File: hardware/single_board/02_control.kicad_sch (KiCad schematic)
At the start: 30 parts, among them U7 RP2350A, U8 W25Q128JVUXIQ, U9 SPX3819M5-3.3, Y1 12MHz

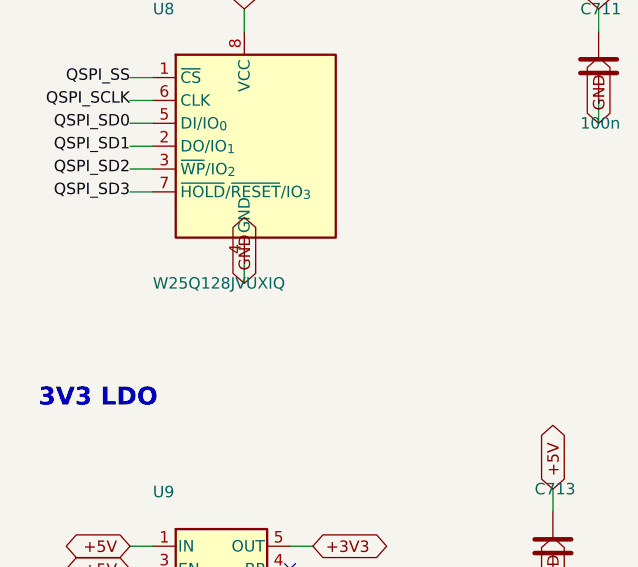
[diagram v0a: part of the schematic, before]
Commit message: Every placed part gets an LCSC number; 3D inductors and part colours fixed
LCSC (hardware/parts/lcsc.csv, 76 rows): every part the assembler places on
boards A (120) and S (173) now has a number, joined into the 3D part pane.
Chosen from the sister board's BOM where it had the part, JLC basic parts
where the rating allowed, each matched to the net it sits on and checked
against JLCPCB's library (model, package, rating, stock) on 2026-09-24. The
notes say why where it was not obvious: 100 V X7R/C0G on VBUS, 0.1% thin
film for the dividers, a Vishay WSL metal-strip jumper for phase C's 0R
(75 A, where a thick-film 0R carries a few), a CL 20 pF crystal for the
27 pF caps, the RGB LED placed rotated 180 deg. export_3d.py warns about any
placed part without a number; copper features (lands, lead pads, bosses)
get no LCSC row in the pane.

Two values changed because nothing stocked matches them:
- Shunts 1m6 -> 2m0 (WSLP20102L000FEA): no 1.6 mOhm 2010 exists at LCSC or
  JLCPCB. The pair is 1.0 mOhm, 50 mV/A, +-29.0 A worst case -- 2.5% over
  the 28.3 A peak, the margin draft 0.3 turned down, taken knowingly.
  geometry.SHUNT_EACH follows; spec, README and status page re-derive the
  sense chain and the loss budget (10.72 W, <= 6.67 K/W, >= 100 cm2).
- Flash W25Q128 -> W25Q16JVUXIQ: no 128 Mbit part comes in USON 2x3; this
  is the RP2350 reference design's part. Derived symbol renamed W25Q16JV.
Schematics regenerated in a scratch copy and only the changed sheets copied
back (diffed: nothing else moved); the routed boards' value fields patched
in place. ERC 0 and DRC 0 on both; KiCad's parity list is HEAD's minus one
(board A's U8 value mismatch). Board S's plan drawings and parts table
regenerated, which also brings them back in line with the final placement.

3D export:
- Board S's two buck inductors were invisible: kicad-cli 9.0.8 meshes a STEP
  that is an assembly of sub-assemblies (KiCad's own SWPA4030S) as empty
  nodes, silently. tools/flatten_step.py flattens it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
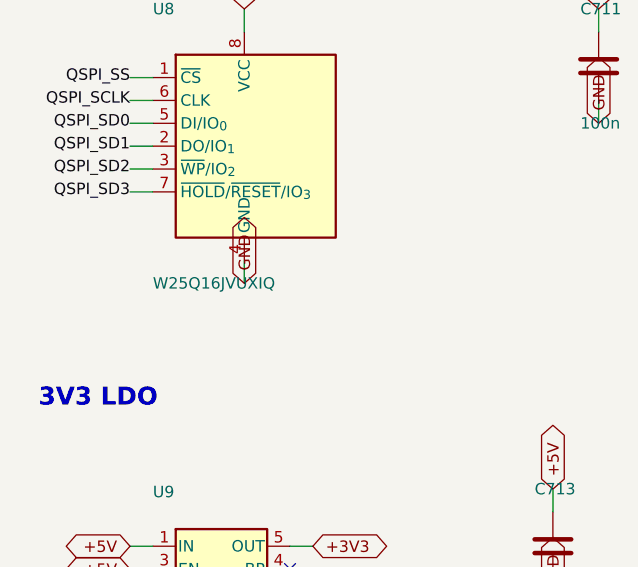
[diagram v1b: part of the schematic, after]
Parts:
- U8: value W25Q128JVUXIQ -> W25Q16JVUXIQ; symbol servodrive:W25Q128JV -> servodrive:W25Q16JV
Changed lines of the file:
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@@
 )
 	(symbol
-		(lib_id "servodrive:W25Q128JV")
+		(lib_id "servodrive:W25Q16JV")
 		(at 38.1000 355.6000 0)
 		(unit 1)
@@
 			(at 27.9400 340.3600 0)
 			(effects (font (size 1.27 1.27)) (justify left)))
-		(property "Value" "W25Q128JVUXIQ"
+		(property "Value" "W25Q16JVUXIQ"
 			(at 27.9400 370.8400 0)
 			(effects (font (size 1.27 1.27)) (justify left)))

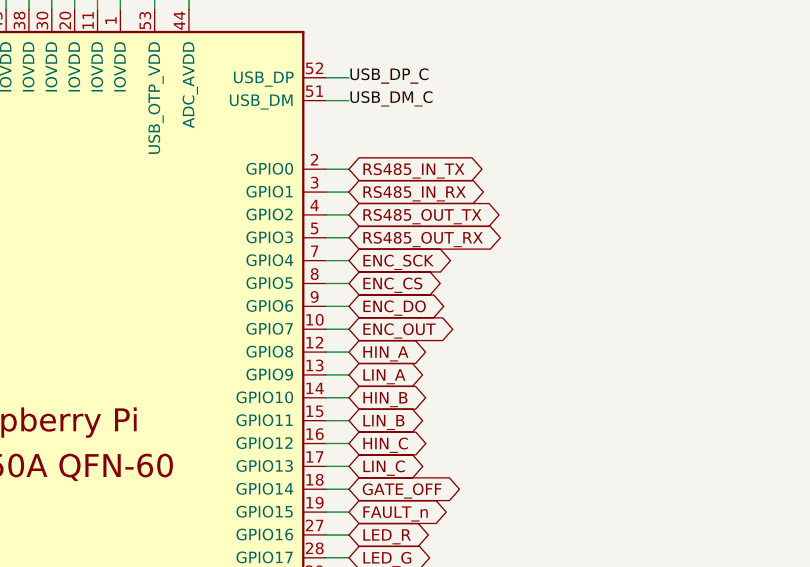
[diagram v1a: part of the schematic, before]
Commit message: Board S: screw keepouts, finer In3 centre rules, encoder on SPI0 (WIP, unrouted)
Work in progress from 2026-09-24/25, saved before routing is finished.
The board file here is the generator's output, not a routed board.

- Keepouts on F.Cu and B.Cu round the four centre motor screws
- USB-C placed tangent to the edge
- Encoder on SPI0 (ENC_DO GPIO4, ENC_SCK GPIO6); J13 pins swapped
- C901 moved north; encoder stitching vias back in the chip's pads
- "fine centre" rule area: signal nets on In3 inside R 17 may use
  0.12 mm track and clearance (servodrive_S.kicad_dru); finish.py's
  maze tries 0.12 there when 0.15 fails; the area is stripped before
  the DSN export so freerouting doesn't see it as a keepout
- Footprint tweaks: 0402 small pads, L_pol_2016, RP2350 QFN

Co-Authored-By: Claude Opus 5.5 (1M context) <noreply@anthropic.com>
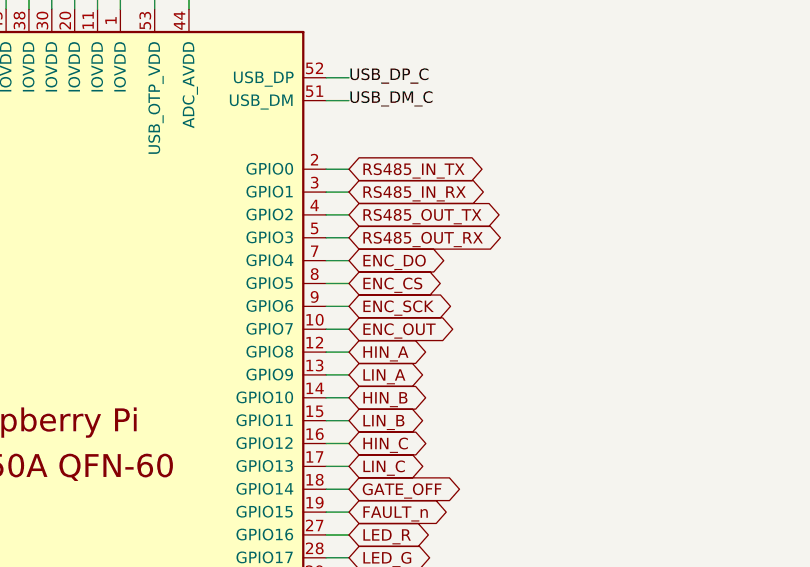
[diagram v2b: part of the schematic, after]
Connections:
- net ENC_DO: now also U7.7 (GPIO4); no longer U7.9 (GPIO6)
- net ENC_SCK: now also U7.9 (GPIO6); no longer U7.7 (GPIO4)
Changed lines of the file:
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@@
 	(wire (pts (xy 91.4400 62.2300) (xy 93.9800 62.2300))
 		(stroke (width 0) (type default)))
-	(global_label "ENC_SCK" (shape bidirectional)
+	(global_label "ENC_DO" (shape bidirectional)
 		(at 93.9800 62.2300 0)
 		(effects (font (size 1.27 1.27)) (justify left))
@@
 	(wire (pts (xy 91.4400 67.3100) (xy 93.9800 67.3100))
 		(stroke (width 0) (type default)))
-	(global_label "ENC_DO" (shape bidirectional)
+	(global_label "ENC_SCK" (shape bidirectional)
 		(at 93.9800 67.3100 0)
 		(effects (font (size 1.27 1.27)) (justify left))

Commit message: Board S schematic: drawn as a person would draw it
The sheets were a grid of parts with a stub and a label on every pin.
tools/schdraw.py now draws a netlist from a hand-written layout: parts
placed and turned, wires between the pins that belong together, T-joins
split with a junction dot, ground and supply symbols on power pins, labels
only where a signal leaves its block. tools/schlayout_s.py is board S's
five sheets: signal left to right, supplies up, ground down, each part's
support parts at the pin they serve, dashed frames and notes.

The drawing cannot change the circuit: every sheet is checked against
schematic_s's netlist before it is written, and `schdraw.py --check s`
compares KiCad's own netlist export net by net (it matches; ERC 0 at all
severities; PCB parity unchanged, same 219 reports as before).

Found on the way: a symbol's instance path must be /<root>/<sheet>. With
the root left out, as schematic.py writes it, KiCad joins labelled nets
but silently drops every net that is only wire.

Co-Authored-By: Claude Opus 5.5 (1M context) <noreply@anthropic.com>
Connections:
- net +3V3A: no longer names the net of C716.1, R703.2, U7.44 (ADC_AVDD)
- net USB_DM_C: no longer names the net of R708.2, U7.51 (USB_DM)
- net USB_DP_C: no longer names the net of R707.2, U7.52 (USB_DP)
- net VREG_AVDD: no longer names the net of C718.1, R706.2, U7.46 (VREG_AVDD)
- net VREG_LX: no longer names the net of L701.2, U7.48 (VREG_LX)
- net XIN: no longer names the net of C709.1, U7.21 (XIN), Y1.1
- net XOUT: no longer names the net of R702.1, U7.22 (XOUT)
- net XTAL2: no longer names the net of C710.1, R702.2, Y1.3
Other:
- note added: "Decoupling"
- note added: "Notes"
- note added: "RP2350A"
- note added: "RP2350A as Raspberry Pi's minimal design (RP-006440): the core supply is the chip's own switching regulator, VREG_LX through L701 to +1V1, which VREG_FB senses and DVDD takes. VREG_AVDD is +3V3 through R706 and C718. One 100n at each IOVDD pin (C701-C706); C714 4u7 at VREG_VIN. ADC_AVDD is +3V3 filtered by R703 and C716 (+3V3A). BOOTSEL: SW1 on sheet 05 pulls QSPI_SS low through R701 at reset. SP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"
- note removed: "ADC supply"
- note removed: "CPU"
- note removed: "USB"
- note removed: "clock"
- note removed: "core rail"
- note removed: "decoupling"
- note removed: "power sources"
- note removed: "reset"
- moved on the sheet: C701, C702, C703, C704, C705, C706, C707, C709, C710, C711, C712, C713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

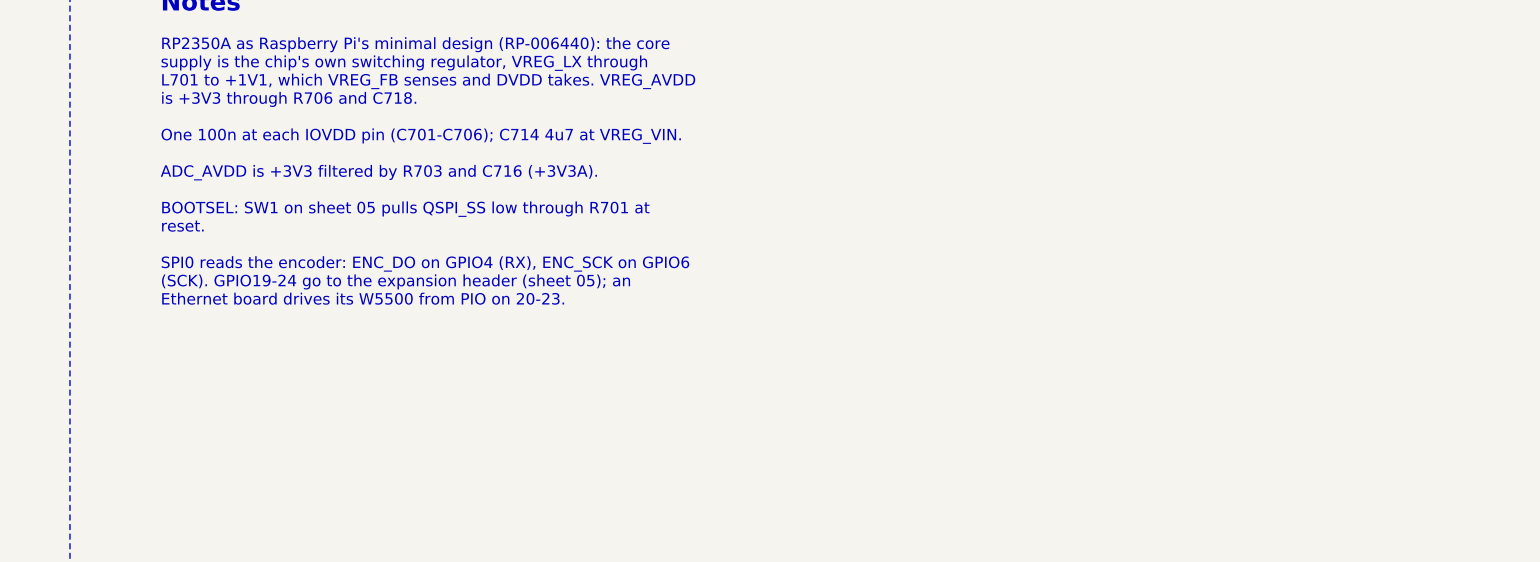
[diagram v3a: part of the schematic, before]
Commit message: Board S schematic: the header and the notes follow the netlist
J13's pins are drawn by net (VBUS row, ground row, supply pins on staggered
stubs, labels for the rest), and the encoder note reads its GPIOs off U7, so
the same layout draws main's pin map and this branch's.

Co-Authored-By: Claude Opus 5.5 (1M context) <noreply@anthropic.com>
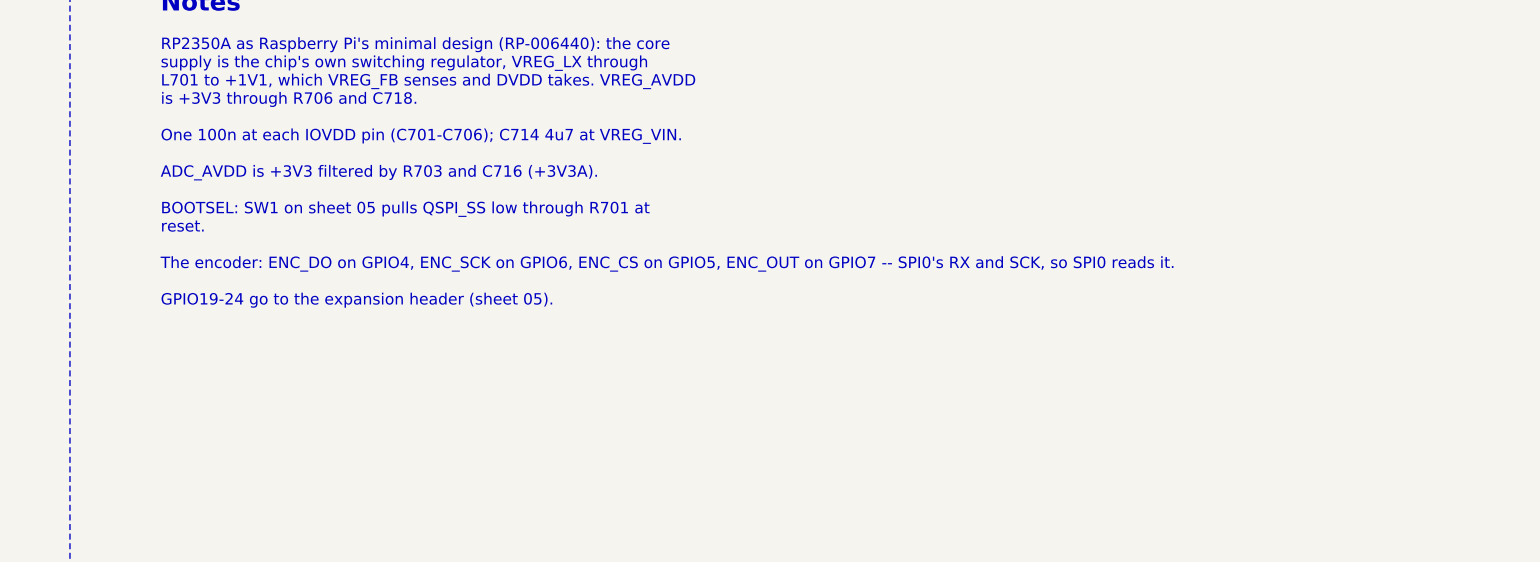
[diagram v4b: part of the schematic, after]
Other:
- note added: "RP2350A as Raspberry Pi's minimal design (RP-006440): the core supply is the chip's own switching regulator, VREG_LX through L701 to +1V1, which VREG_FB senses and DVDD takes. VREG_AVDD is +3V3 through R706 and C718. One 100n at each IOVDD pin (C701-C706); C714 4u7 at VREG_VIN. ADC_AVDD is +3V3 filtered by R703 and C716 (+3V3A). BOOTSEL: SW1 on sheet 05 pulls QSPI_SS low through R701 at reset. Th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"
- note removed: "RP2350A as Raspberry Pi's minimal design (RP-006440): the core supply is the chip's own switching regulator, VREG_LX through L701 to +1V1, which VREG_FB senses and DVDD takes. VREG_AVDD is +3V3 through R706 and C718. One 100n at each IOVDD pin (C701-C706); C714 4u7 at VREG_VIN. ADC_AVDD is +3V3 filtered by R703 and C716 (+3V3A). BOOTSEL: SW1 on sheet 05 pulls QSPI_SS low through R701 at reset. SP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"
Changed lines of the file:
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@@
 	(generator "eeschema")
 	(generator_version "9.0")
-	(paper "A3")
+	(paper "A2")
 	(title_block (title "servodrive — board S, single board — 02_control") (date "2026-09-25") (rev "A")
 		(company "Sequoia Hope Alexander")
@@
 		(effects (font (size 2.0 2.0) (bold yes)) (justify left top))
 )
-	(text "RP2350A as Raspberry Pi's minimal design (RP-006440): the core\nsupply is the chip's own switching regulator, VREG_LX through\nL701 to +1V1, which VREG_FB senses and DVDD takes. VREG_AVDD\nis +3V3 through R706 and C718.\n\nOne 100n at each IOVDD pin (C701-C706); C714 4u7 at VREG_VIN.\n\nADC_AVDD is +3V3 filtered by R703 and C716 (+3V3A).\n\nBOOTSEL: SW1 on sheet 05 pulls QSPI_SS low through R701 at\nreset.\n\nSPI0 reads the encoder: ENC_DO on GPIO4 (RX), ENC_SCK on GPIO6\n(SCK). GPIO19-24 go to the expansion header (sheet 05); an\nEthernet board drives its W5500 from PIO on 20-23." (exclude_from_sim no)
+	(text "RP2350A as Raspberry Pi's minimal design (RP-006440): the core\nsupply is the chip's own switching regulator, VREG_LX through\nL701 to +1V1, which VREG_FB senses and DVDD takes. VREG_AVDD\nis +3V3 through R706 and C718.\n\nOne 100n at each IOVDD pin (C701-C706); C714 4u7 at VREG_VIN.\n\nADC_AVDD is +3V3 filtered by R703 and C716 (+3V3A).\n\nBOOTSEL: SW1 on sheet 05 pulls QSPI_SS low through R701 at\nreset.\n\nThe encoder: ENC_DO on GPIO4, ENC_SCK on GPIO6, ENC_CS on GPIO5, ENC_OUT on GPIO7 -- SPI0's RX and SCK, so SPI0 reads it.\n\nGPIO19-24 go to the expansion header (sheet 05)." (exclude_from_sim no)
 		(at 287.0200 97.7900 0)
 		(effects (font (size 1.27 1.27)) (justify left top))

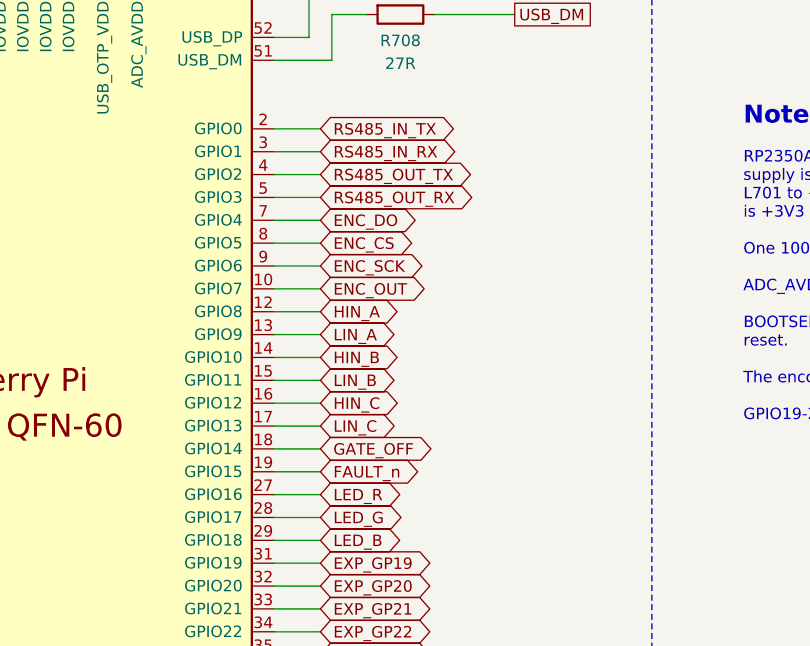
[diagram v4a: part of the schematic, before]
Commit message: Board S: GATE_OFF and FAULT_n to GPIO2/3, port OUT's PIO UART to 14/15 (unrouted)
On GPIO14/15, GATE_OFF and FAULT_n left the RP2350 on the side facing away
from Q1001 and R705; with keepouts round the motor screws that side's
corridor was one track short, and every router and rip-up left one of
GATE_OFF, FAULT_n, RUN or LED_R open. GPIO0-3 are the pads nearest Q1001,
and port OUT's transceivers sit on 14/15's side. A PIO UART takes any
pins; GPIO2 is pulled down through reset as 14 was, so the gate rail still
comes up braking.

Board regenerated, not yet routed. Netlist check, KiCad netlist export and
ERC clean.

Co-Authored-By: Claude Opus 5.5 (1M context) <noreply@anthropic.com>
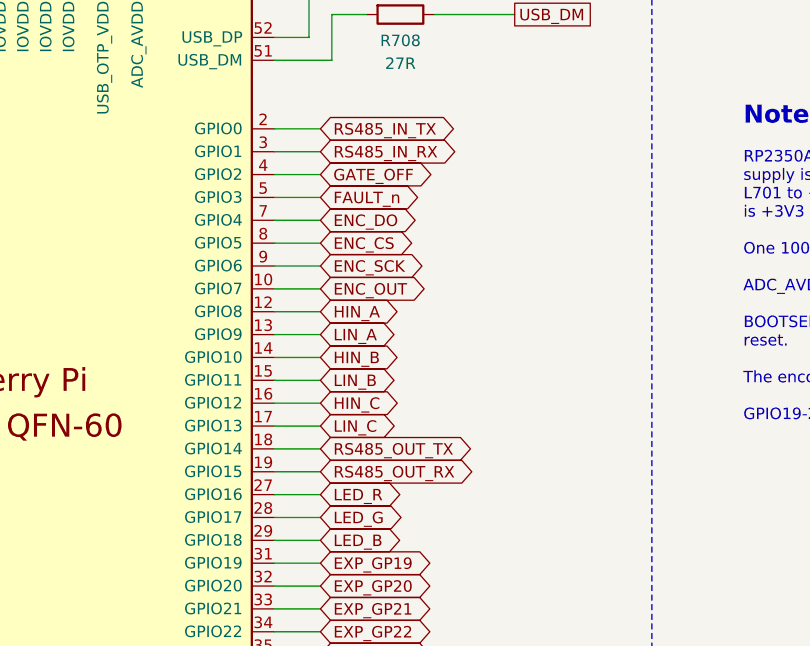
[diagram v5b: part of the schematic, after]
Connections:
- net FAULT_n: now also U7.5 (GPIO3); no longer U7.19 (GPIO15)
- net GATE_OFF: now also U7.4 (GPIO2); no longer U7.18 (GPIO14)
- net RS485_OUT_RX: now also U7.19 (GPIO15); no longer U7.5 (GPIO3)
- net RS485_OUT_TX: now also U7.18 (GPIO14); no longer U7.4 (GPIO2)
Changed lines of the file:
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@@
 			(at 240.0300 128.2700 0)
 			(effects (font (size 1.27 1.27)) (hide yes))))
-	(global_label "GATE_OFF" (shape bidirectional)
+	(global_label "RS485_OUT_TX" (shape bidirectional)
 		(at 240.0300 130.8100 0)
 		(effects (font (size 1.27 1.27)) (justify left))
@@
 			(at 240.0300 130.8100 0)
 			(effects (font (size 1.27 1.27)) (hide yes))))
-	(global_label "FAULT_n" (shape bidirectional)
+	(global_label "RS485_OUT_RX" (shape bidirectional)
 		(at 240.0300 133.3500 0)
 		(effects (font (size 1.27 1.27)) (justify left))
@@
 			(at 240.0300 158.7500 0)
 			(effects (font (size 1.27 1.27)) (hide yes))))
-	(global_label "RS485_OUT_TX" (shape bidirectional)
+	(global_label "GATE_OFF" (shape bidirectional)
 		(at 240.0300 100.3300 0)
 		(effects (font (size 1.27 1.27)) (justify left))
@@
 			(at 240.0300 171.4500 0)
 			(effects (font (size 1.27 1.27)) (hide yes))))
-	(global_label "RS485_OUT_RX" (shape bidirectional)
+	(global_label "FAULT_n" (shape bidirectional)
 		(at 240.0300 102.8700 0)
 		(effects (font (size 1.27 1.27)) (justify left))
